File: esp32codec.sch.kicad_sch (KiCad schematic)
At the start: 7 parts, among them U13 TL072, U4 NAU88C22YG

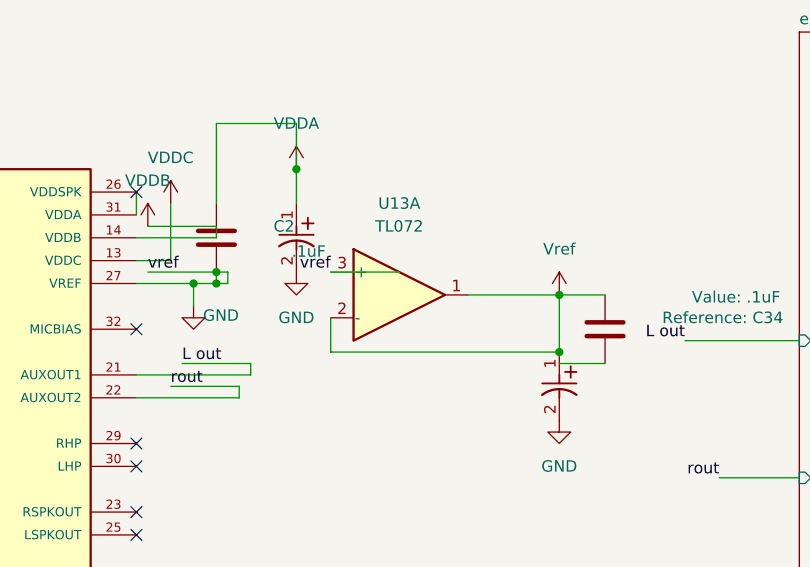
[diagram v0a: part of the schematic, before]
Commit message: updated a few caps
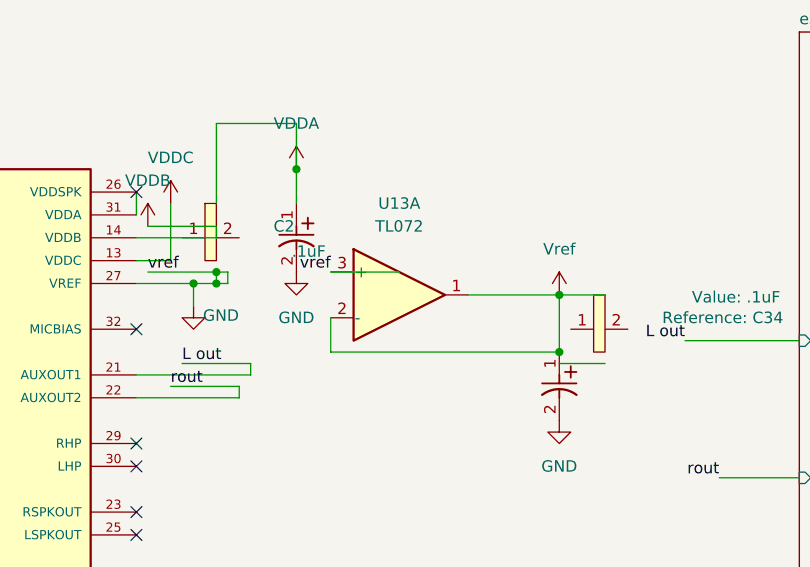
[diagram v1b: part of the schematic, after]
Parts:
- C2, C34: footprint Capacitor_SMD:C_0201_0603Metric -> commonfootprint:Ceramic0603; symbol Device:C -> common:CerCap
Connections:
- net GND: no longer C2.2
- net VDDA: no longer C2.1
- net Vref: no longer C34.1
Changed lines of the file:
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@@
 	)
 	(symbol
-		(lib_id "Device:C")
+		(lib_id "common:CerCap")
 		(at 191.77 83.82 0)
 		(unit 1)
@@
 			)
 		)
-		(property "Footprint" "Capacitor_SMD:C_0201_0603Metric"
+		(property "Footprint" "commonfootprint:Ceramic0603"
 			(at 192.7352 87.63 0)
 			(effects
@@
 	)
 	(symbol
-		(lib_id "Device:C")
+		(lib_id "common:CerCap")
 		(at 148.59 73.66 0)
 		(unit 1)
@@
 			)
 		)
-		(property "Footprint" "Capacitor_SMD:C_0201_0603Metric"
+		(property "Footprint" "commonfootprint:Ceramic0603"
 			(at 149.5552 77.47 0)
 			(effects
